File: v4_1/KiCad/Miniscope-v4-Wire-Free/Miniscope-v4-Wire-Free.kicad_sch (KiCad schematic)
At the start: 114 parts, among them J1 0475710001, J10 Conn_01x01, J11 Conn_01x01, J12 Conn_01x01, J14 Conn_01x01, J15 Conn_01x01, J16 Conn_01x01, J17 Conn_01x01, J18 Conn_01x01, J19 Conn_01x01, J2 Conn_01x04, J20 Conn_01x01, J21 Conn_01x01, J22 Conn_01x01, J23 Conn_01x01, J24 Conn_01x01, J25 Conn_01x01, J26 Conn_01x01, J27 Conn_01x01, J3 Conn_01x04, J4 Conn_01x01, J5 Conn_01x01, J6 Conn_01x01, J7 Conn_01x01, J8 Conn_01x01, J9 Conn_01x01, Q1 NTK3134NT1G, Q2 MMBT3904LP-7B, SW1 TL3780AF330QG, U1 LTC3554, U2 HV892, U3 LTC3218, U4 MAX13030EETE+BGA, U5 TSOP57438TT1, U6 ATSAMD51J20A-UUT-EFP, U7 NCP163AMX330TBG, U8 NOIP1SN0480A, U9 LMV321IDCKR, Y2 Crystal

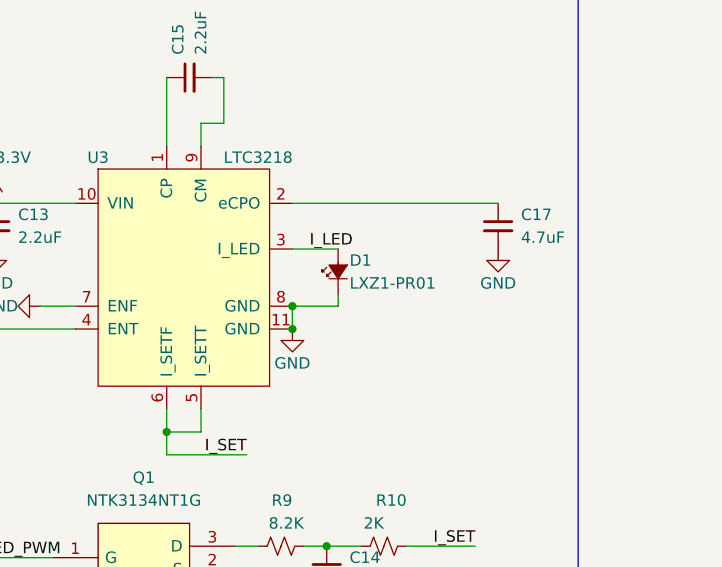
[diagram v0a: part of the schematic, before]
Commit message: Modification to the Programming cable PCB and firmware
- Corrected the footprint and layout of the programming cable PCB. Switched from a 100 mil pogo pin connector to the correct size (50 mil)
- Cleaned and built the firmware for flashing to the MCU
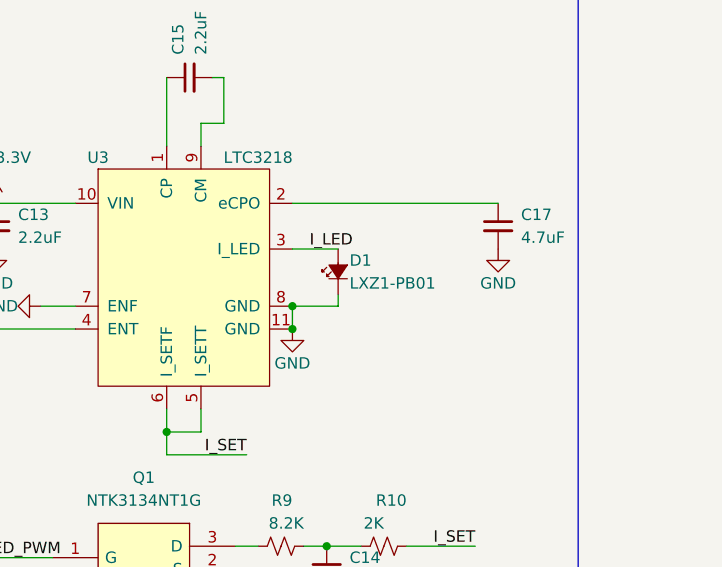
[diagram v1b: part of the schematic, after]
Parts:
- C1, C2, C26, C35, C50, C51, C52, C6, C7: Manufacturer_Name (none) -> Murata; Manufacturer_Part_Number (none) -> GRM155R60J106ME15D
- C16: Manufacturer_Name (none) -> Murata; Manufacturer_Part_Number (none) -> GCM188R72A472KA37D
- D1: value LXZ1-PR01 -> LXZ1-PB01; Manufacturer_Name (none) -> Lumileds; Manufacturer_Part_Number (none) -> LXZ1-PB01
- J1: Manufacturer_Name (none) -> Molex; Manufacturer_Part_Number (none) -> 0475710001
- J2, J3, R12: Manufacturer_Name (none) -> DNL; Manufacturer_Part_Number (none) -> DNL
- L1, L5: Manufacturer_Name (none) -> TDK; Manufacturer_Part_Number (none) -> MLZ1608N100LT000
- L2: Manufacturer_Name (none) -> Abracon; Manufacturer_Part_Number (none) -> ASMCI-0805-4R7M-T
- L3, L4: Manufacturer_Name (none) -> Murata; Manufacturer_Part_Number (none) -> BLM18PG471SN1D
- Q2: Manufacturer_Name (none) -> Diodes Incorporated; Manufacturer_Part_Number (none) -> MMBT3904LP-7B
- R1, R17: Manufacturer_Name (none) -> Vishay Dale; Manufacturer_Part_Number (none) -> CRCW020124K9FNED
- R10: Manufacturer_Name (none) -> Vishay Dale; Manufacturer_Part_Number (none) -> CRCW02012K00FNED
- R11, R19: Manufacturer_Name (none) -> Vishay Dale; Manufacturer_Part_Number (none) -> CRCW02011K00FKED
- R13: Manufacturer_Name (none) -> Panasonic; Manufacturer_Part_Number (none) -> ERJ-1GNF4023C
- R14, R16, R20: Manufacturer_Name (none) -> Panasonic; Manufacturer_Part_Number (none) -> ERJ-1GNF1003C
- R15: Manufacturer_Name (none) -> Panasonic; Manufacturer_Part_Number (none) -> ERJ-1GNF3742C
- R21: Manufacturer_Name (none) -> Vishay Dale; Manufacturer_Part_Number (none) -> CRCW020147K5FNED
- R3: Manufacturer_Name (none) -> Vishay Dale; Manufacturer_Part_Number (none) -> CRCW02011M27FNED
- R4: Manufacturer_Name (none) -> Vishay Dale; Manufacturer_Part_Number (none) -> CRCW02012M05FNED
- R5: Manufacturer_Name (none) -> Vishay Dale; Manufacturer_Part_Number (none) -> CRCW02011M00FNED
- R6: Manufacturer_Name (none) -> Vishay Dale; Manufacturer_Part_Number (none) -> CRCW0201649KFNED
- R7, R8: Manufacturer_Name (none) -> Panasonic; Manufacturer_Part_Number (none) -> ERJ-1GNF2201C
- R9: Manufacturer_Name (none) -> Vishay Dale; Manufacturer_Part_Number (none) -> CRCW02018K20FKED
- SW1: Manufacturer_Name (none) -> E-Switch; Manufacturer_Part_Number (none) -> TL3780AF330QG
- U1: Manufacturer_Name (none) -> Analog Devices Inc.
- U2: Manufacturer_Name (none) -> Microchip; Manufacturer_Part_Number (none) -> HV892K7-G
- U3: Manufacturer_Name (none) -> Analog Devices Inc.; Manufacturer_Part_Number (none) -> LTC3218
- U4: Manufacturer_Name (none) -> Maxim Integrated; Manufacturer_Part_Number (none) -> MAX13030EETE+
- U5: Manufacturer_Name (none) -> Vishay Semiconductor Opto Division; Manufacturer_Part_Number (none) -> TSOP57438TT1
- U6: Manufacturer_Name (none) -> Microchip; Manufacturer_Part_Number (none) -> ATSAMD51J20A-UUT-EFP
- U7: Manufacturer_Name (none) -> onsemi; Manufacturer_Part_Number (none) -> NCP163AMX330TBG
- U8: Manufacturer_Name (none) -> onsemi; Manufacturer_Part_Number (none) -> NOIP1SN0480A-STI1
